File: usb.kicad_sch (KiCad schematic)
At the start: 36 parts, among them J1 USB_C_Receptacle_USB2.0_14P, U15 AMS1117-3.3, U2 SRV05-4, U3 M24C02-WMN, U4 CH334F, U5 CH217K, Y1 12Mhz

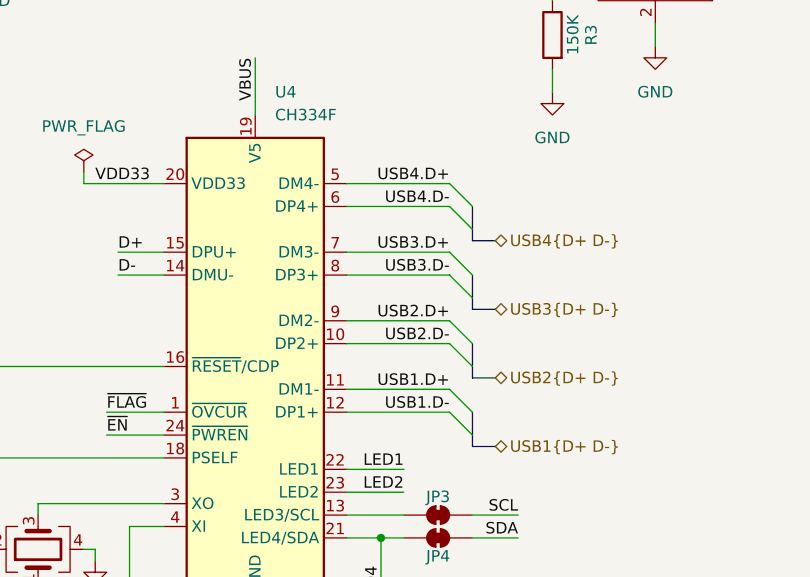
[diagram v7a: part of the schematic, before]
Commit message: Fix rev1 errors
Add USB mux to allow for USB PIO
Fix D+ D- mixup
Fix USB Hub LED indicator label
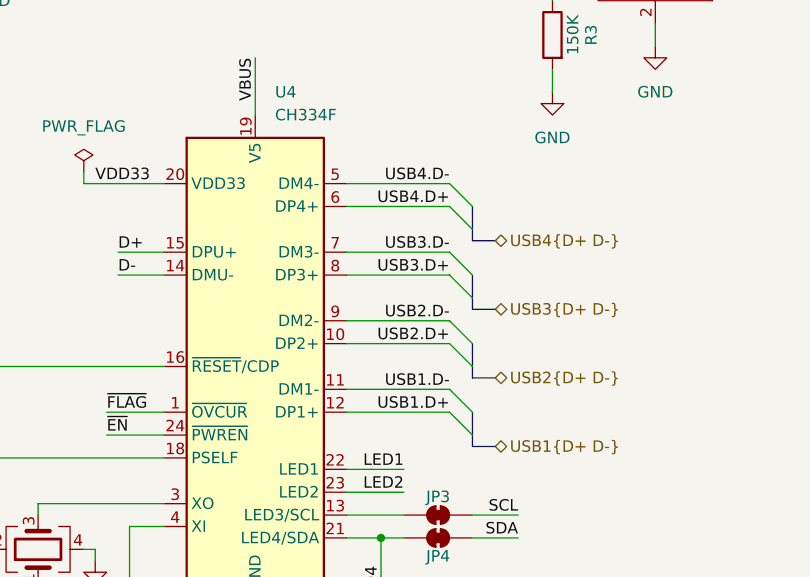
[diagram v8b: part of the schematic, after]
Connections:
- net USB1.D+: now also U4.12 (DP1+); no longer U4.11 (DM1-)
- net USB1.D-: now also U4.11 (DM1-); no longer U4.12 (DP1+)
- net USB2.D+: now also U4.10 (DP2+); no longer U4.9 (DM2-)
- net USB2.D-: now also U4.9 (DM2-); no longer U4.10 (DP2+)
- net USB3.D+: now also U4.8 (DP3+); no longer U4.7 (DM3-)
- net USB3.D-: now also U4.7 (DM3-); no longer U4.8 (DP3+)
- net USB4.D+: now also U4.6 (DP4+); no longer U4.5 (DM4-)
- net USB4.D-: now also U4.5 (DM4-); no longer U4.6 (DP4+)
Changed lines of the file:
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@@
 		)
 	)
-	(label "USB1.D-"
+	(label "USB1.D+"
 		(at 173.99 88.9 180)
 		(effects
@@
 		)
 	)
+	(label "USB3.D-"
+		(at 173.99 71.12 180)
+		(effects
+			(font
+				(size 1.27 1.27)
+			)
+			(justify right bottom)
+		)
+	)
+	(label "USB2.D+"
+		(at 173.99 81.28 180)
+		(effects
+			(font
+				(size 1.27 1.27)
+			)
+			(justify right bottom)
+		)
+	)
+	(label "USB2.D-"
+		(at 173.99 78.74 180)
+		(effects
+			(font
+				(size 1.27 1.27)
+			)
+			(justify right bottom)
+		)
+	)
 	(label "USB3.D+"
-		(at 173.99 71.12 180)
-		(effects
-			(font
-				(size 1.27 1.27)
-			)
-			(justify right bottom)
-		)
-	)
-	(label "USB2.D-"
-		(at 173.99 81.28 180)
-		(effects
-			(font
-				(size 1.27 1.27)
-			)
-			(justify right bottom)
-		)
-	)
-	(label "USB2.D+"
-		(at 173.99 78.74 180)
-		(effects
-			(font
-				(size 1.27 1.27)
-			)
-			(justify right bottom)
-		)
-	)
-	(label "USB3.D-"
 		(at 173.99 73.66 180)
 		(effects
@@
 		)
 	)
-	(label "USB4.D-"
+	(label "USB4.D+"
 		(at 173.99 66.04 180)
 		(effects
@@
 		)
 	)
-	(label "USB4.D+"
+	(label "USB4.D-"
 		(at 173.99 63.5 180)
 		(effects
@@
 		)
 	)
-	(label "USB1.D+"
+	(label "USB1.D-"
 		(at 173.99 86.36 180)
 		(effects
